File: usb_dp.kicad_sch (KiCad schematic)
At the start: 59 parts, among them J9 USB-C_WE_632723300011, U30 TPS65988DHRSHR, U33 TUSB1046-DCIRNQ, U35 AP22615A_TSOT26, U36 TPD4E05U06QDQARQ1, U37 TPD4E05U06QDQARQ1, U38 TPD4E05U06QDQARQ1, U41 TPD4E05U06QDQARQ1

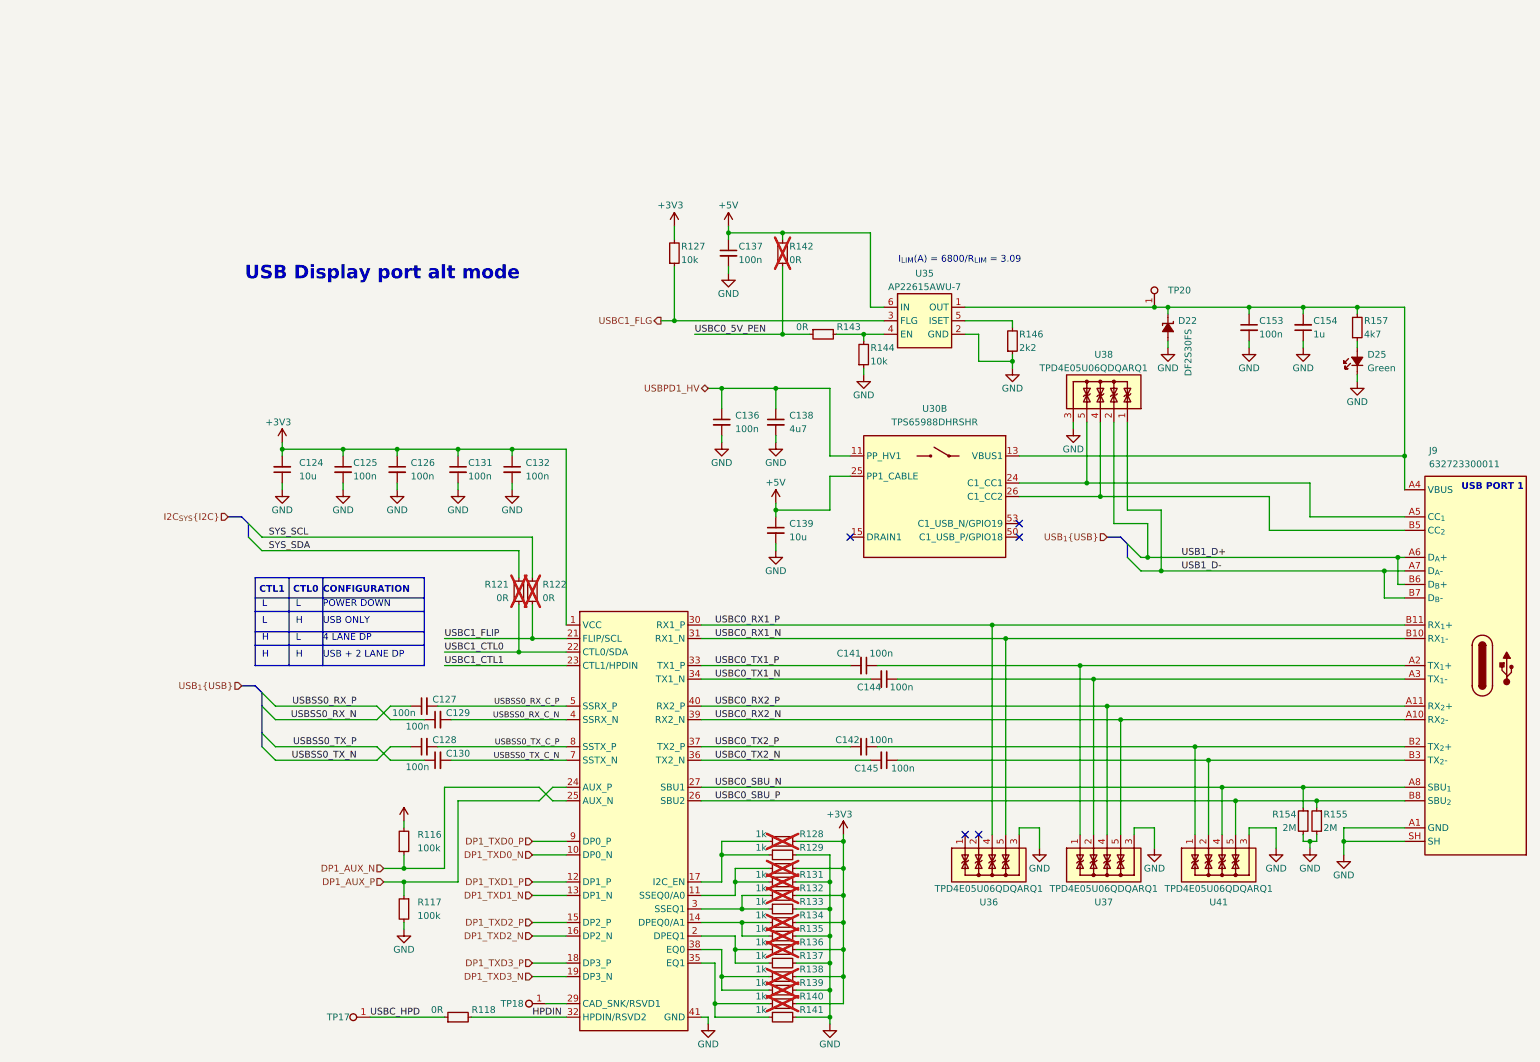
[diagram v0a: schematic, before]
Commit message: [#82837] Start fixing USB DP Alt mode sheet: clean up, define DP bus, rename USB nets and buses to match rest of the schematic
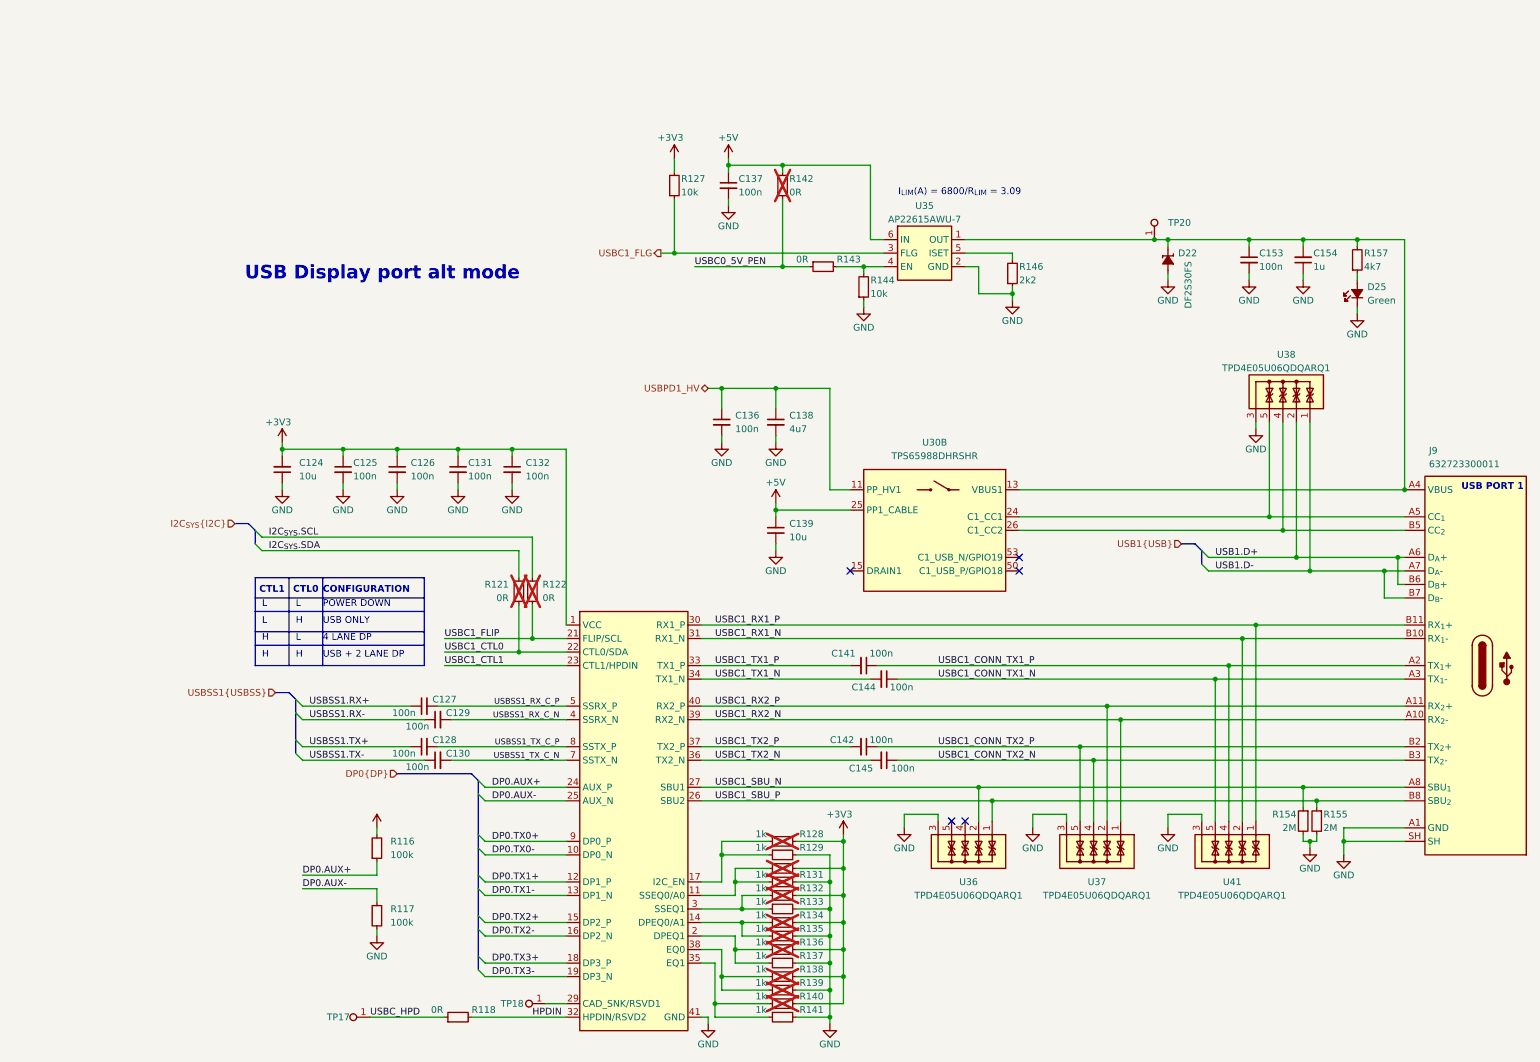
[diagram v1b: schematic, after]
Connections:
- net USBC1_CONN_TX2_P: now reaches C142.1, J9.B2 (TX_{2}+)
- net USBC1_CONN_TX2_P: now also U37.5, U37.6; no longer U41.1, U41.10
- net USBC1_CONN_TX2_N: now reaches C145.1, J9.B3 (TX_{2}-)
- net USBC1_CONN_TX2_N: now also U37.4, U37.7; no longer U41.2, U41.9
- net USBC1_SBU_P: now reaches U36.1, U36.10
- net USBC1_SBU_P: now also J9.B8 (SBU_{2}), R155.1, U33.26 (SBU2)
- net USBC1_SBU_N: now reaches U36.2, U36.9
- net USBC1_SBU_N: now also J9.A8 (SBU_{1}), R154.1, U33.27 (SBU1)
- net USBC1_CONN_TX1_N: now reaches C144.1, J9.A3 (TX_{1}-)
- net USBC1_CONN_TX1_N: now also U41.5, U41.6; no longer U37.2, U37.9
- net USBC1_CONN_TX1_P: now reaches C141.1, J9.A2 (TX_{1}+)
- net USBC1_CONN_TX1_P: now also U41.4, U41.7; no longer U37.1, U37.10
- net DP1_AUX_N renamed DP0.AUX+
- net DP0.AUX+: now also U33.24 (AUX_P); no longer U33.25 (AUX_N)
- net DP1_AUX_P renamed DP0.AUX-
- net DP0.AUX-: now also U33.25 (AUX_N); no longer U33.24 (AUX_P)
- net DP1_TXD0_N renamed DP0.TX0-
- net DP1_TXD0_P renamed DP0.TX0+
- net DP1_TXD1_N renamed DP0.TX1-
- net DP1_TXD1_P renamed DP0.TX1+
- net DP1_TXD2_N renamed DP0.TX2-
- net DP1_TXD2_P renamed DP0.TX2+
- net DP1_TXD3_N renamed DP0.TX3-
- net DP1_TXD3_P renamed DP0.TX3+
- net SYS_SCL renamed I2C_{SYS}.SCL
- net SYS_SDA renamed I2C_{SYS}.SDA
- net USB1_D+ renamed USB1.D+
- net USB1_D- renamed USB1.D-
- net USBC0_RX1_N: no longer names the net of U36.5, U36.6
- net USBC0_RX1_N: no longer J9.B10 (RX_{1}-), U33.31 (RX1_N)
- net USBC0_RX1_P: no longer names the net of U36.4, U36.7
- net USBC0_RX1_P: no longer J9.B11 (RX_{1}+), U33.30 (RX1_P)
- net USBC0_RX2_N renamed USBC1_RX2_N
- net USBC1_RX2_N: now also U37.1, U37.10; no longer U37.5, U37.6
- net USBC0_RX2_P renamed USBC1_RX2_P
- net USBC1_RX2_P: now also U37.2, U37.9; no longer U37.4, U37.7
- removed net USBC0_SBU_N: J9.A8 (SBU_{1}), R154.1, U33.27 (SBU1), U41.4, U41.7
- removed net USBC0_SBU_P: J9.B8 (SBU_{2}), R155.1, U33.26 (SBU2), U41.5, U41.6
- net USBC0_TX1_N renamed USBC1_TX1_N
- net USBC0_TX1_P renamed USBC1_TX1_P
- net USBC0_TX2_N renamed USBC1_TX2_N
- net USBC0_TX2_P renamed USBC1_TX2_P
- net USBSS0_RX_C_N renamed USBSS1_RX_C_N
- net USBSS0_RX_C_P renamed USBSS1_RX_C_P
- net USBSS0_RX_N renamed USBSS1.RX+
- net USBSS0_RX_P renamed USBSS1.RX-
- net USBSS0_TX_C_N renamed USBSS1_TX_C_N
- net USBSS0_TX_C_P renamed USBSS1_TX_C_P
- net USBSS0_TX_N renamed USBSS1.TX+
- net USBSS0_TX_P renamed USBSS1.TX-
- new net USBC1_RX1_N: J9.B10 (RX_{1}-), U33.31 (RX1_N), U41.2, U41.9
- new net USBC1_RX1_P: J9.B11 (RX_{1}+), U33.30 (RX1_P), U41.1, U41.10
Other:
- moved on the sheet: C137, C153, C154, D22, D25, R116, R117, R127, R142, R143, R144, R146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

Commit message: [#82837] Start rerouting USB PD controller
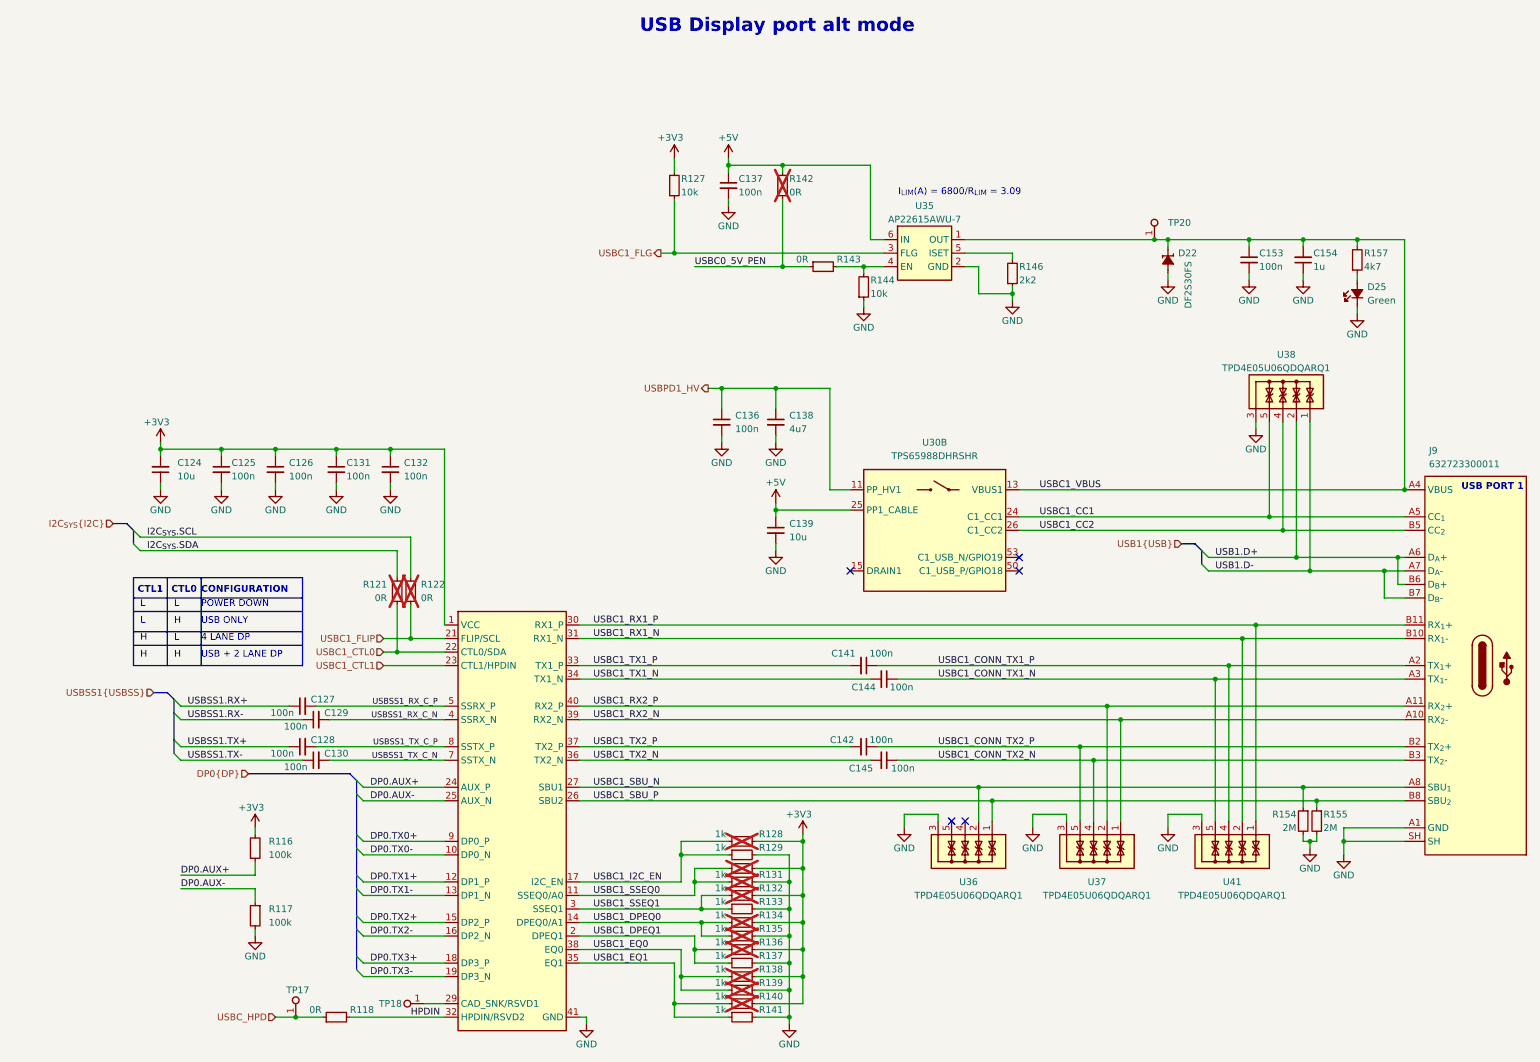
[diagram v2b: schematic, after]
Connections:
- net USBC1_DPEQ0: now reaches R134.1, R135.1, U33.14 (DPEQ0/A1)
- net USBC1_DPEQ1: now reaches R136.1, R137.1, U33.2 (DPEQ1)
- net USBC1_I2C_EN: now reaches R128.1, R129.1, U33.17 (I2C_EN)
- net USBC1_VBUS: now reaches C153.1, C154.2, D22.1 (C), J9.A4 (VBUS), J9.A9 (VBUS), J9.B4 (VBUS), J9.B9 (VBUS), R157.2, TP20.1, U30.13 (VBUS1), U35.1 (OUT)
- net USBC1_SSEQ0: now reaches R130.1, R131.1, U33.11 (SSEQ0/A0)
- net USBC1_SSEQ1: now reaches R132.1, R133.1, U33.3 (SSEQ1)
- net USBC1_EQ1: now reaches R140.1, R141.1, U33.35 (EQ1)
- net USBC1_EQ0: now reaches R138.1, R139.1, U33.38 (EQ0)
- net USBC1_CC2: now reaches J9.B5 (CC_{2}), U30.26 (C1_CC2), U38.4, U38.7
- net USBC1_CC1: now reaches J9.A5 (CC_{1}), U30.24 (C1_CC1), U38.5, U38.6
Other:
- moved on the sheet: C124, C125, C126, C127, C128, C129, C130, C131, C132, R116, R117, R118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

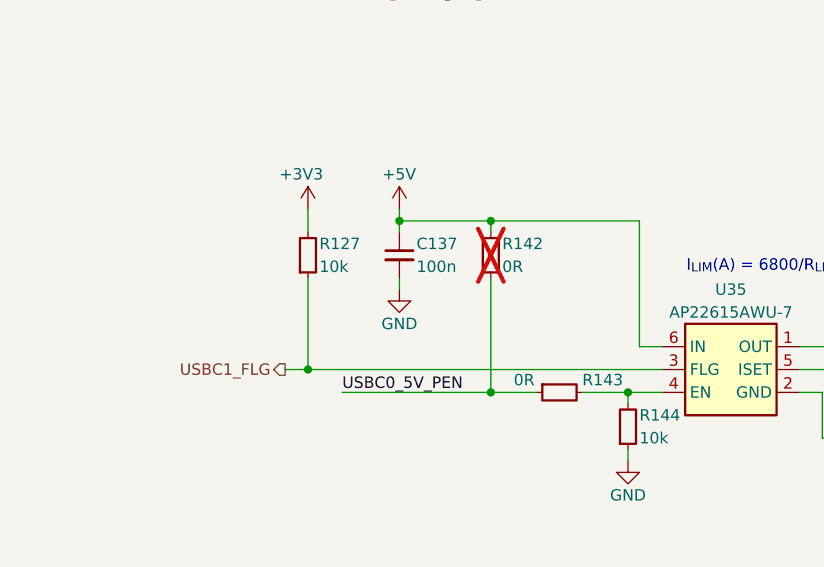
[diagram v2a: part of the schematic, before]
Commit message: [#82837] Prepare schematic to add root connections to USB section
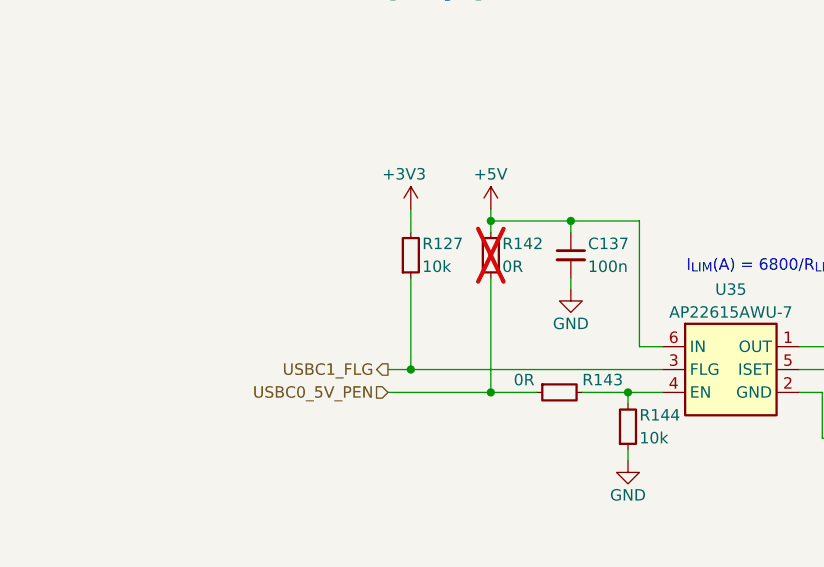
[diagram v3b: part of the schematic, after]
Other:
- moved on the sheet: C137, R127

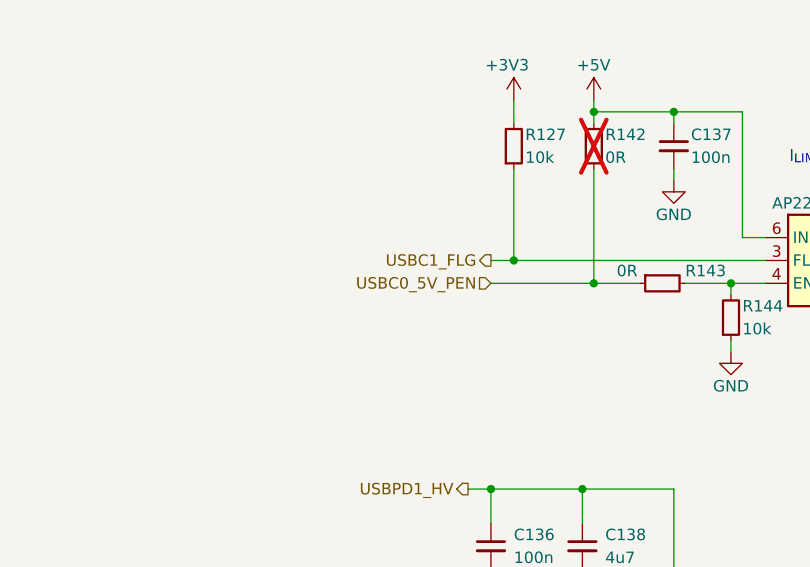
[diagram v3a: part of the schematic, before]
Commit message: [#82837] Finish mapping interfaces, waiting for new SoM symbol
[#82837] Add GPIO level shifter and route USB related GPIO on root
schematic

[#82837] WIP: Modify Power-up and reset section
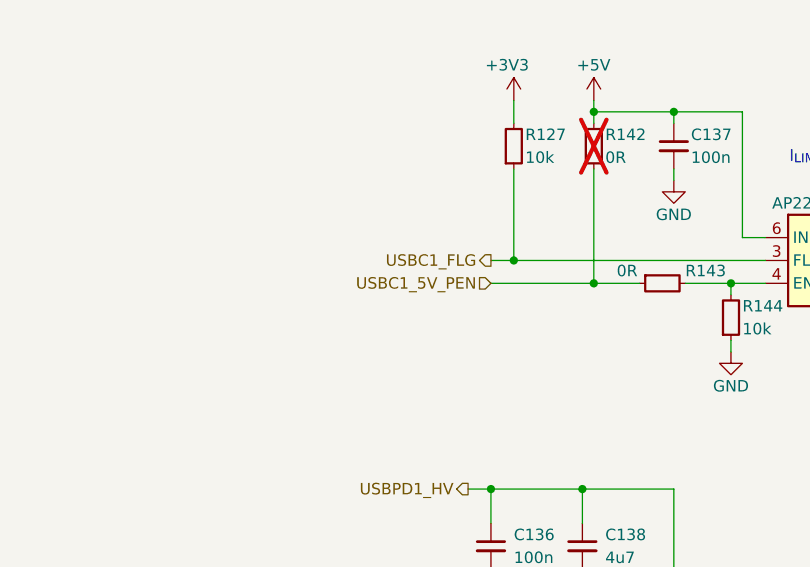
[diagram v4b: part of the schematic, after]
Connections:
- net USBC0_5V_PEN renamed USBC1_5V_PEN
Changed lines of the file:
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@@
 		)
 	)
-	(hierarchical_label "USBC0_5V_PEN"
+	(hierarchical_label "USBC1_5V_PEN"
 		(shape input)
 		(at 177.8 68.58 180)

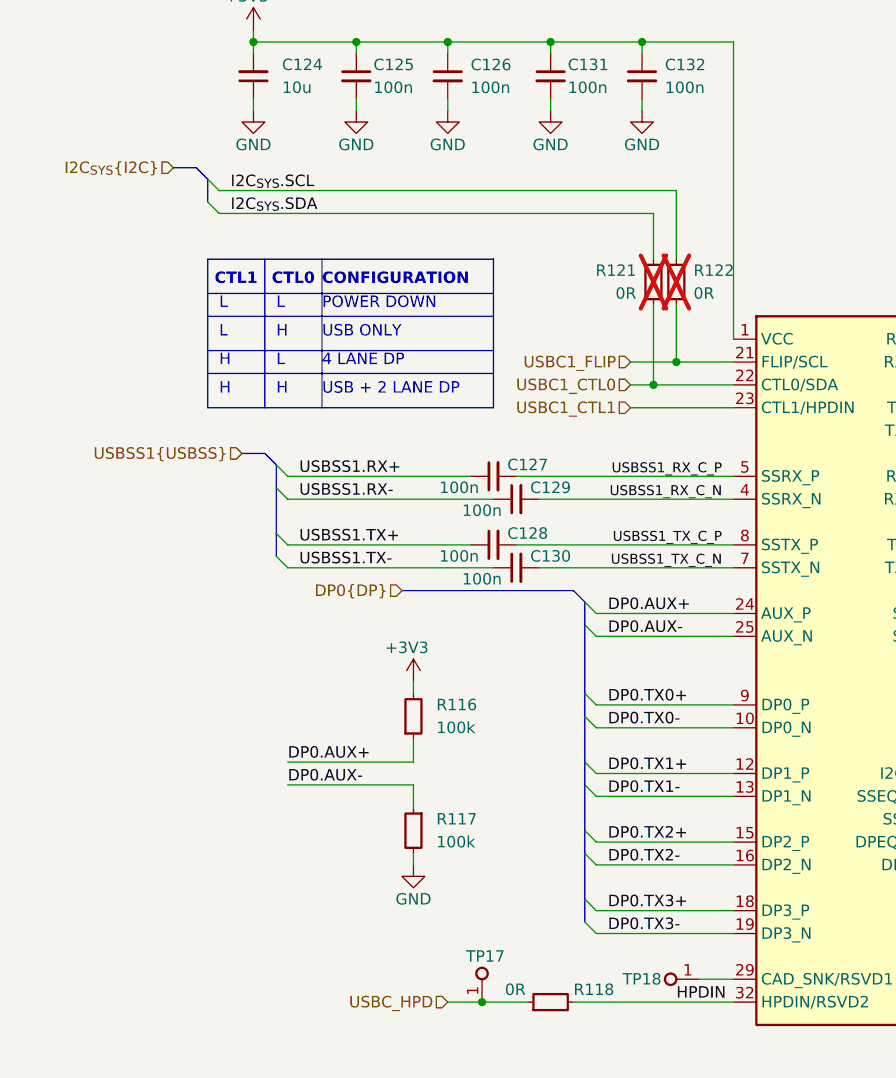
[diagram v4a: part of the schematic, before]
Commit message: [#82837] Finish mapping PCIe and SFP+ connections on SoM
[#82837] WIP: correct ERC errors

[#82837] WIP: correct ERC errors, fix signal direction of most buses

[#82837] Fix all ERC errors
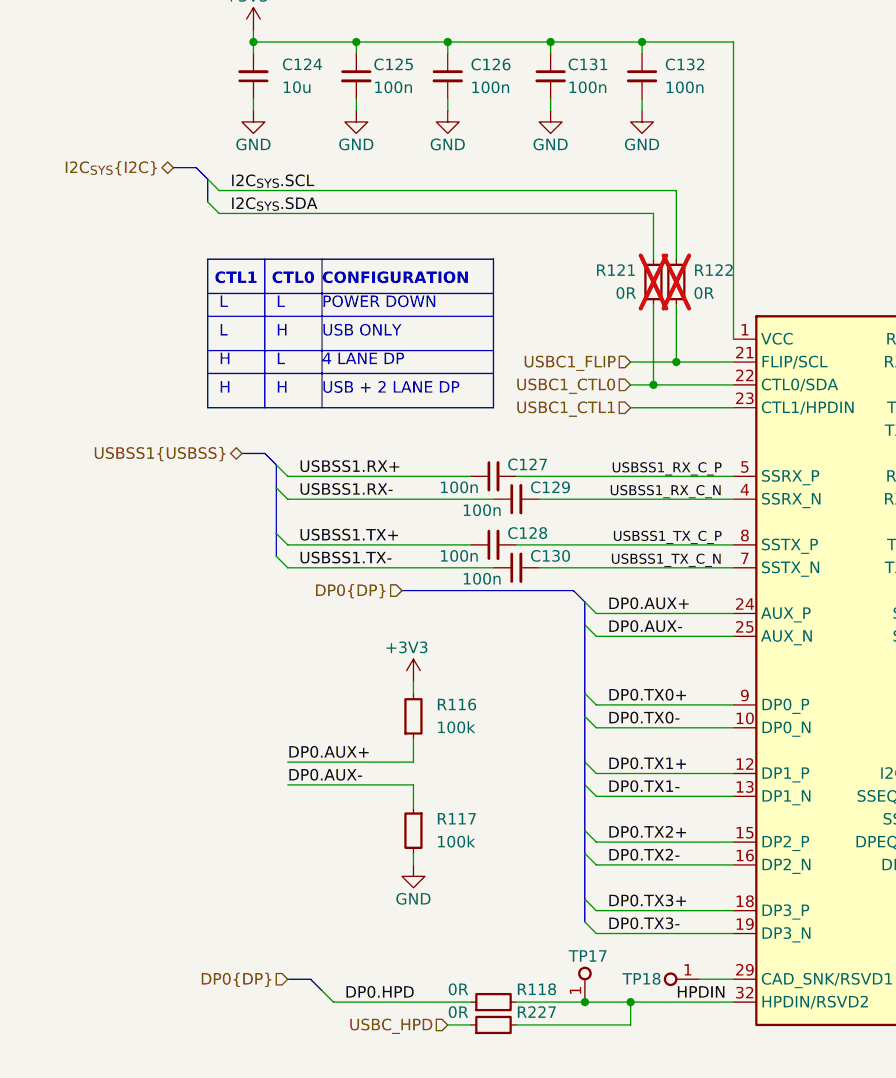
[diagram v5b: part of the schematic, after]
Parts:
- added R227: R_0R_0402, antmicro-footprints:R_0402_1005Metric, symbol antmicroResistors0402:R_0R_0402
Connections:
- net HPDIN: now also TP17.1, R227.2
- net USBC_HPD: now also R227.1; no longer R118.1, TP17.1
- new net DP0.HPD: R118.1
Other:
- moved on the sheet: R118, TP17
